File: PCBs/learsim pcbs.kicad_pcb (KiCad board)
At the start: 2 copper layers, 120 x 110 mm, 53 parts, among them SW1 MHz, SW2 KHz, SW3 2MS1T1B1M2QES-5, U1 ESP32-C6-DEV-KIT-N8, U2 MAX7219, U3 MAX7219

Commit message: Refactor code structure for improved readability and maintainability
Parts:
- removed SW3: 2MS1T1B1M2QES-5, Rotary:SW-TH_2MS1T1B1M2QES-5
- added C6: 220uF, Capacitor_THT:CP_Radial_D6.3mm_P2.50mm, B.Cu at (81.2, 36.0)
- added SW4: 2MD1T1B1M2QES-5, Rotary:SW-TH_2MD1T1B1M2QES-5, F.Cu at (44.9, 92.0)
- R15, R16: moved to B.Cu
- moved U3 93.7 mm to (34.2, 55.3), turned to 90 degrees
- moved R2 46.9 mm to (66.8, 47.7), turned to -90 degrees
- moved R1 45.6 mm to (112.2, 59.2), turned to 0 degrees
- moved U2 38.6 mm to (99.6, 55.6), turned to 90 degrees
- moved R15 1.46 mm to (47.9, 98.0)
- moved R14 1.27 mm to (132.2, 48.5)
- moved R16 0.75 mm to (41.6, 98.2)
- turned D1 to 0 degrees
- turned D2 to 0 degrees
- turned D3 to 0 degrees
- turned D4 to 0 degrees
- turned D6 to 0 degrees
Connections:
- D1 pad 2: LED_DIN -> LED_12
- D1 pad 4: LED_12 -> LED_23
- D2 pad 2: LED_12 -> LED_23
- D2 pad 4: LED_23 -> LED_34
- D3 pad 2: LED_23 -> LED_34
- D3 pad 4: LED_34 -> LED_45
- D4 pad 2: LED_34 -> LED_45
- D4 pad 4: LED_45 -> LED_56
- D5 pad 2: LED_45 -> LED_DIN
- D5 pad 4: LED_56 -> LED_12
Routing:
- net +5V: track 0.00 -> 497.1 mm, vias 0 -> 2
- net +3V3: track 0.00 -> 352.9 mm, vias 0 -> 4
- net SPI_CLK: track 0.00 -> 142.0 mm
- net BTN_COM1: track 0.00 -> 107.3 mm, vias 0 -> 3
- net SPI_LOAD: track 0.00 -> 101.4 mm, vias 0 -> 1
- net SW3_B: track 0.00 -> 98.9 mm, vias 0 -> 2
- net SW3_A: track 0.00 -> 96.3 mm
- net BTN_COM2: track 0.00 -> 82.7 mm, vias 0 -> 1
- net MAX_CHAIN: track 0.00 -> 73.6 mm
- net ENC2_SW: track 0.00 -> 72.1 mm, vias 0 -> 2
- net SPI_DIN: track 0.00 -> 71.2 mm, vias 0 -> 1
- net BTN_Switch1: track 0.00 -> 68.3 mm
- net LED_12: track 0.00 -> 63.9 mm, vias 0 -> 2
- net ENC2_B: track 0.00 -> 59.9 mm, vias 0 -> 1
- net BTN_ADF1: track 0.00 -> 57.6 mm, vias 0 -> 1
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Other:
- board text added: "Axel Draws"
- board text added: "Learsim 2026"
- board text added: "Radio Panel"

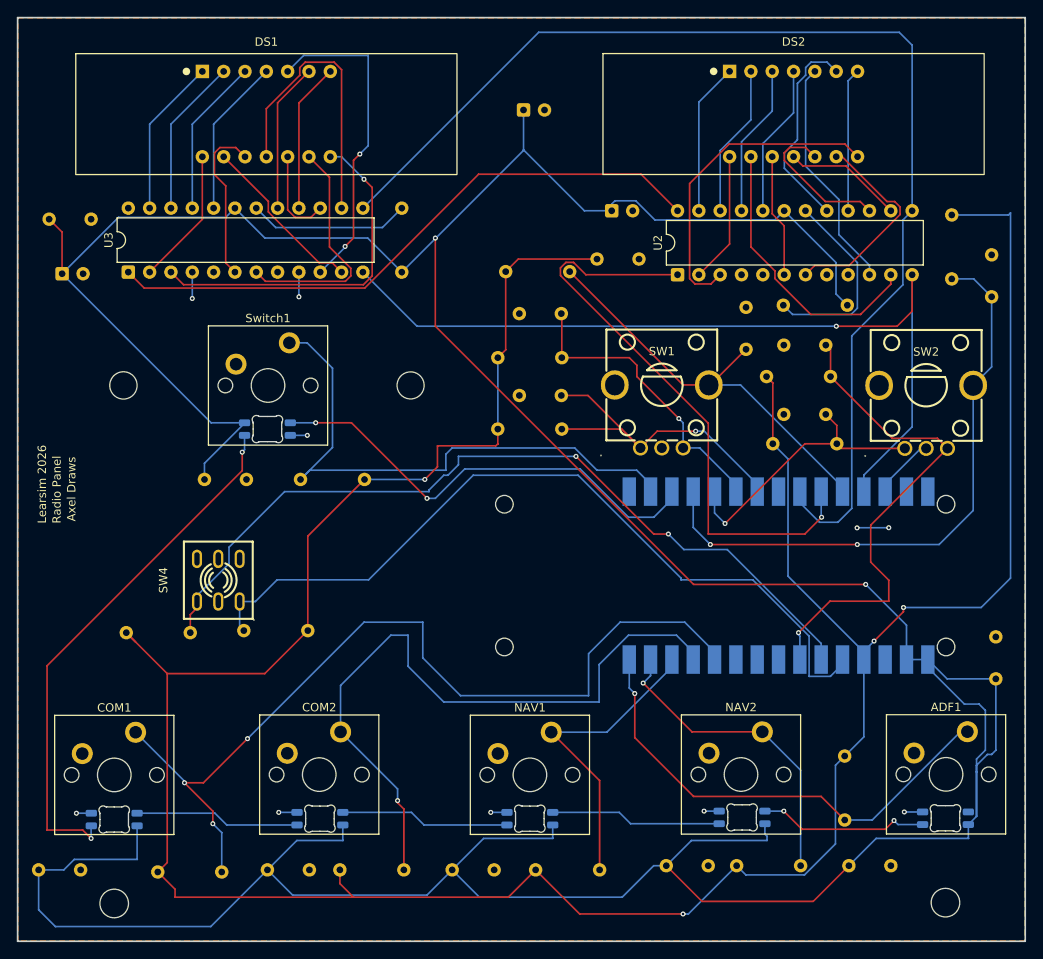
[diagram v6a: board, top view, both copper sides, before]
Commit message: Update drill files and job configuration with new timestamps and adjustments
- Updated creation dates in NPTH and PTH drill files to 2026-07-26.
- Adjusted coordinates for several drill points in NPTH file for improved accuracy.
- Modified drill sizes in PTH file, changing T2 from 0.700 to 0.650.
- Added new coordinates in PTH file for additional drill points.
- Updated creation date in job configuration file to 2026-07-26.
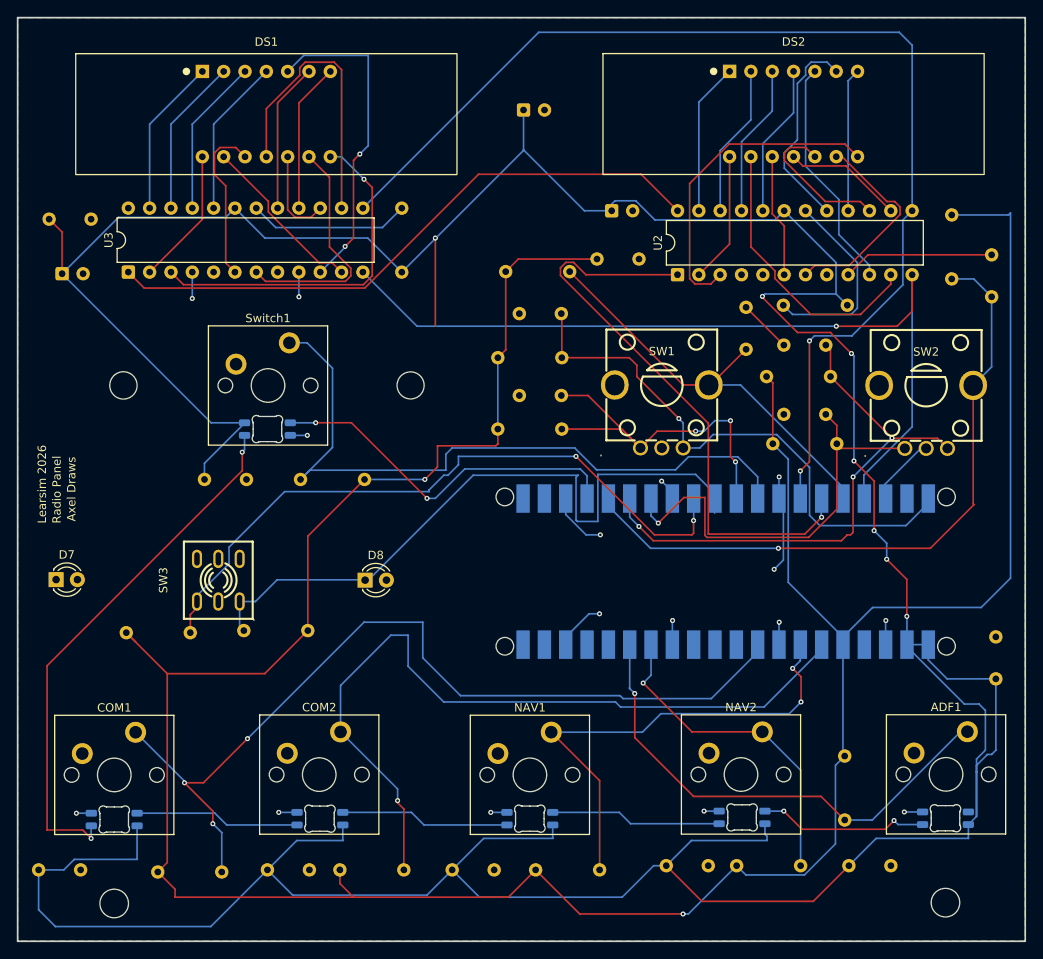
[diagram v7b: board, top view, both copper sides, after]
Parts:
- added D7: COM1 LED, LED_THT:LED_D3.0mm, F.Cu at (25.6, 91.9)
- added D8: COM2 LED, LED_THT:LED_D3.0mm, F.Cu at (62.4, 92.0)
- moved U1 0.48 mm to (105.3, 91.0)
- renumbered SW4 to SW3
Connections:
- U1 pad 1: unconnected-(U1-TX-Pad1) -> ENC1_B
- U1 pad 10: ENC1_B -> ENC1_A
- U1 pad 11: ENC2_A -> SW3_A
- U1 pad 12: ENC2_SW -> SW3_B
- U1 pad 13: LED_DIN -> GND
- U1 pad 14: BTN_Switch1 -> ENC2_A
- U1 pad 15: unconnected-(U1-EXIO7-Pad15) -> ENC2_B
- U1 pad 16: +5V -> ENC2_SW
- U1 pad 17: +5V -> LED_DIN
- U1 pad 18: unconnected-(U1-EN-Pad18) -> GND
- U1 pad 19: +3V3 -> unconnected-(U1-EXIO6-Pad19)
- U1 pad 20: SW3_A -> unconnected-(U1-EXIO7-Pad20)
- U1 pad 21: SW3_B -> +5V
- U1 pad 22: ENC2_B -> +5V
- U1 pad 23: unconnected-(U1-GPIO23_SCL_TCA9554-Pad23) -> GND
- U1 pad 25: unconnected-(U1-RUN-Pad25) -> +3V3
- U1 pad 26: BTN_COM1 -> BTN_COM2
- U1 pad 27: BTN_COM2 -> BTN_NAV1
- U1 pad 28: BTN_NAV1 -> GND
- U1 pad 29: BTN_NAV2 -> BTN_COM1
- U1 pad 30: BTN_ADF1 -> unconnected-(U1-GPIO3-Pad30)
- U1 pad 8: unconnected-(U1-GPIO14-Pad8) -> GND
- U1 pad 9: ENC1_A -> BTN_Switch1
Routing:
- net GND: track 29.4 -> 87.7 mm, vias 10 -> 16
- net ENC1_B: track 35.7 -> 66.1 mm
- net BTN_NAV1: track 37.3 -> 57.6 mm, vias 0 -> 2
- net SW3_B: track 98.9 -> 80.7 mm
- net ENC2_A: track 33.9 -> 52.0 mm
- net BTN_Switch1: track 68.3 -> 83.7 mm
- net SW3_A: track 96.3 -> 82.6 mm
- net BTN_COM2: track 82.7 -> 94.0 mm
- net LED_DIN: track 54.8 -> 43.6 mm
- net +5V: track 497.1 -> 486.5 mm, vias 2 -> 7
- net ENC2_SW: track 72.1 -> 80.0 mm, vias 2 -> 1
- net ENC2_B: track 59.9 -> 65.1 mm, vias 1 -> 3
- net SPI_CLK: track 142.0 -> 138.3 mm, vias 0 -> 2
- net ENC1_A: track 40.6 -> 44.0 mm, vias 1 -> 3
- net BTN_ADF1: track 57.6 -> 59.4 mm
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
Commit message: Update drill files and job configuration with new creation timestamps and modified drill sizes
- Updated creation timestamps in NPTH and PTH drill files to 2026-07-26T23:00:48.
- Adjusted drill sizes for T4, T5, and T6 in the PTH drill file.
- Added new coordinates in the PTH drill file for improved component placement.
- Updated creation date in the job configuration file to 2026-07-26T23:00:53.
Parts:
- added R17: 150, Resistor_THT:R_Axial_DIN0207_L6.3mm_D2.5mm_P7.62mm_Horizontal, B.Cu at (26.6, 84.3)
- added R18: 470, Resistor_THT:R_Axial_DIN0207_L6.3mm_D2.5mm_P7.62mm_Horizontal, B.Cu at (65.0, 97.5)
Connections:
- D7 pad 1: unconnected-(D7-K-Pad1) -> GND
- D7 pad 2: unconnected-(D7-A-Pad2) -> Net-(D7-A)
- D8 pad 1: unconnected-(D8-K-Pad1) -> GND
- D8 pad 2: unconnected-(D8-A-Pad2) -> Net-(D8-A)
- U1 pad 2: unconnected-(U1-RX-Pad2) -> COM2_LED
- U1 pad 30: unconnected-(U1-GPIO3-Pad30) -> COM1_LED
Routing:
- net COM2_LED: track 0.00 -> 108.8 mm, vias 0 -> 5
- net COM1_LED: track 0.00 -> 89.8 mm, vias 0 -> 4
- net +5V: track 486.5 -> 476.0 mm, vias 7 -> 6
- net Net-(D7-A): track 0.00 -> 8.29 mm
- net GND: track 87.7 -> 94.7 mm, vias 16 -> 19
- net Net-(D8-A): track 0.00 -> 6.20 mm
- net BTN_COM1: track 106.9 -> 100.9 mm
- net BTN_COM2: track 94.0 -> 88.8 mm
- net +3V3: track 351.5 -> 349.9 mm
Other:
- board text added: "v1.0"
